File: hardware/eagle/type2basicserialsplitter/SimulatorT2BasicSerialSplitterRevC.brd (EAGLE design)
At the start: 82.5 x 78.7 mm, 35 parts, among them IC1 7805X, IC2 MAX3323DIP, IC3 MAX208DIP

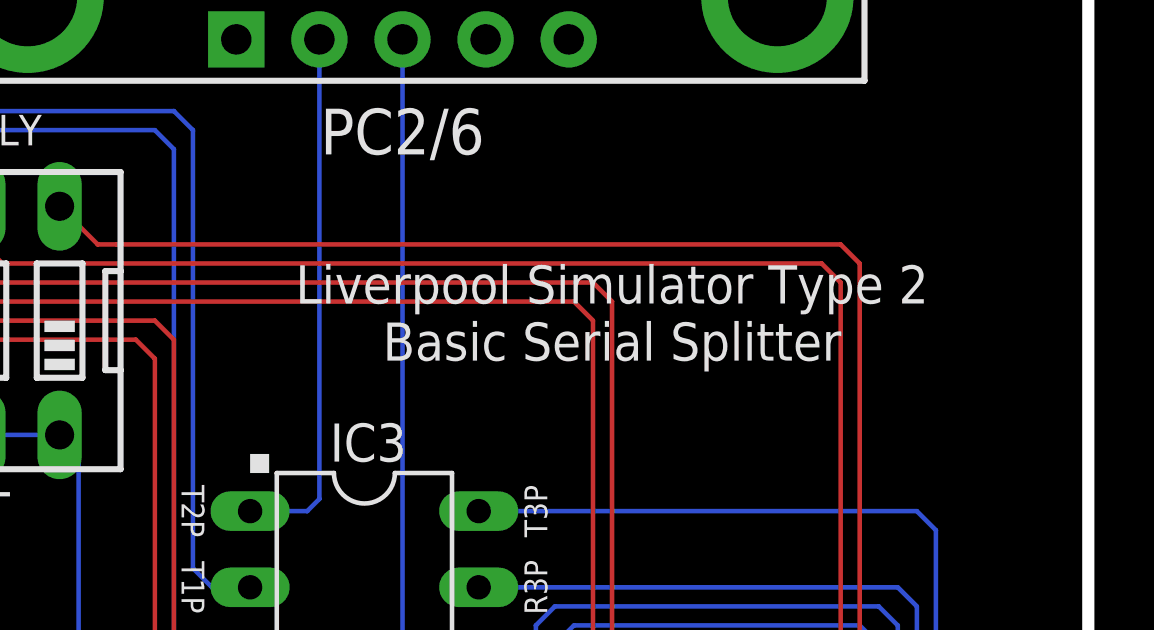
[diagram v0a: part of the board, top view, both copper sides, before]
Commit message: Board Housekeeping
URL on silkscreens, caution messages, tidy up naming conventions.
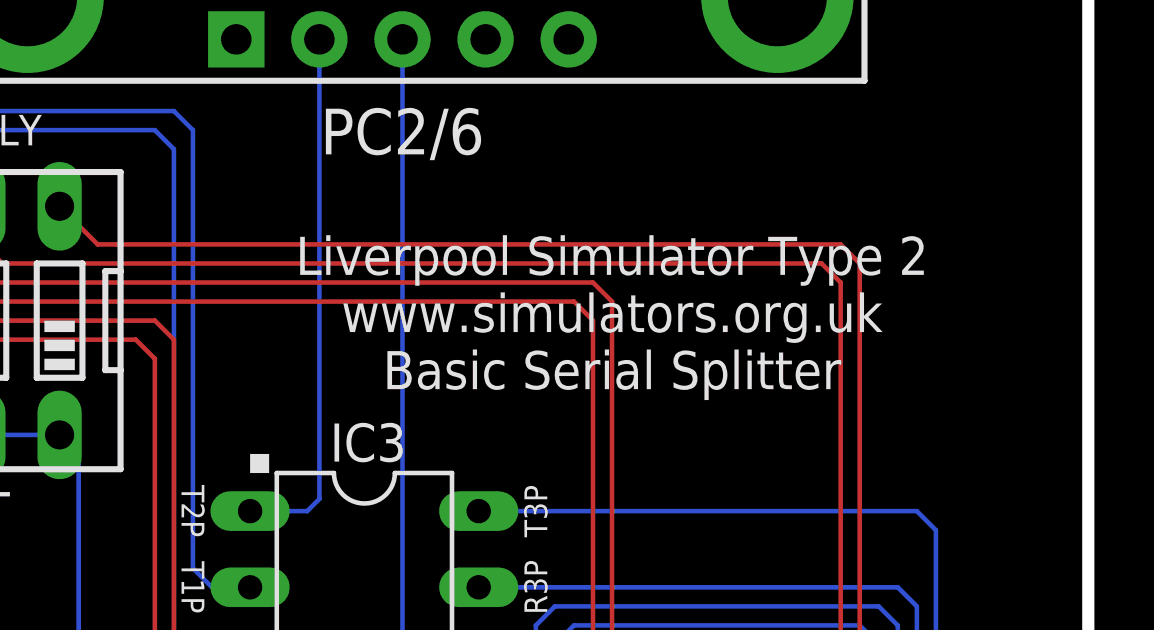
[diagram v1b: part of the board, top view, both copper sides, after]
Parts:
- added U$1: (no value), AIC_Custom:WARNING_TRIANGLE_TPLACE
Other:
- board text added: "Connect this board to Liverpool Simulator Type 2 or compatible equipment ONLY. Refer to documentation for details."
- board text added: "Liverpool Simulator Type 2 www.simulators.org.uk Basic Serial Splitter"
- board text removed: "Liverpool Simulator Type 2 Basic Serial Splitter"
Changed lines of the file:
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@@
 <plain>
 <text x="65.405" y="51.054" size="1.27" layer="21" font="vector" align="center">Liverpool Simulator Type 2
+www.simulators.org.uk
 Basic Serial Splitter</text>
 <text x="77.1525" y="14.6685" size="1.016" layer="21" font="vector" rot="R90" align="center">Rev C
@@
 <dimension x1="92.71" y1="67.31" x2="92.71" y2="-3.81" x3="96.52" y3="31.75" textsize="1.778" layer="47"/>
 <rectangle x1="34.29" y1="35.56" x2="34.925" y2="36.195" layer="21"/>
+<text x="76.2" y="34.29" size="1.27" layer="22" font="vector" rot="MR270" align="center">Connect this board to Liverpool Simulator
+Type 2 or compatible equipment ONLY.
+Refer to documentation for details.</text>
 </plain>
 <attributes>
@@
 <attribute name="VALUE" x="44.069" y="9.525" size="1.27" layer="21" font="vector" rot="R180" align="bottom-center"/>
 </element>
+<element name="U$1" library="AIC_Custom" package="WARNING_TRIANGLE_TPLACE" value="" x="73.66" y="7.62" rot="MR90"/>
 </elements>
 <signals>
